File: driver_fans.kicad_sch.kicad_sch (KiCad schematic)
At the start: 8 parts, among them Q3 PMV60ENEAR

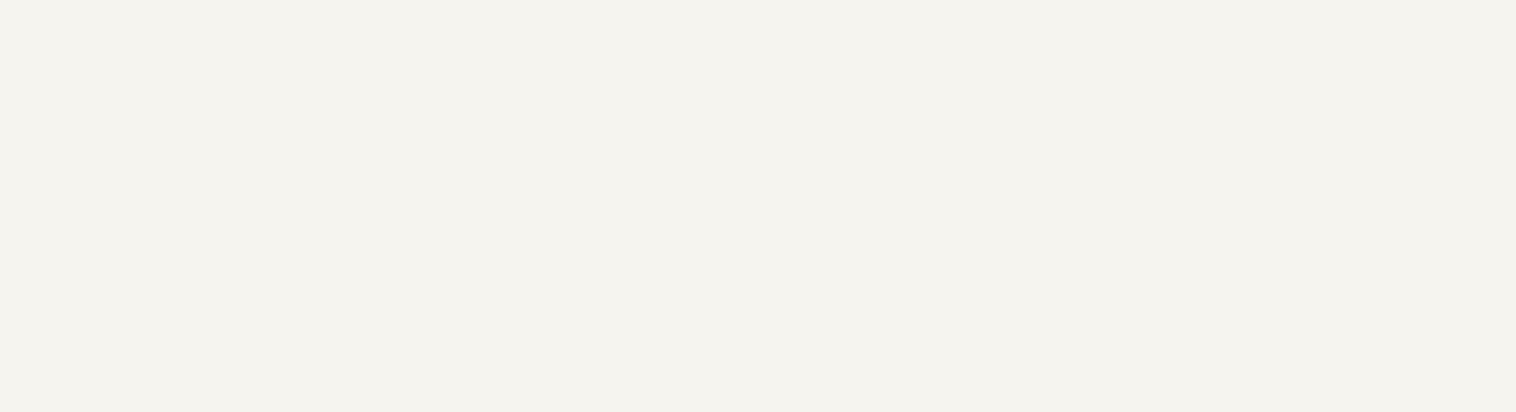
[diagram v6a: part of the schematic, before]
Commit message: added notes section to bottom of sheets
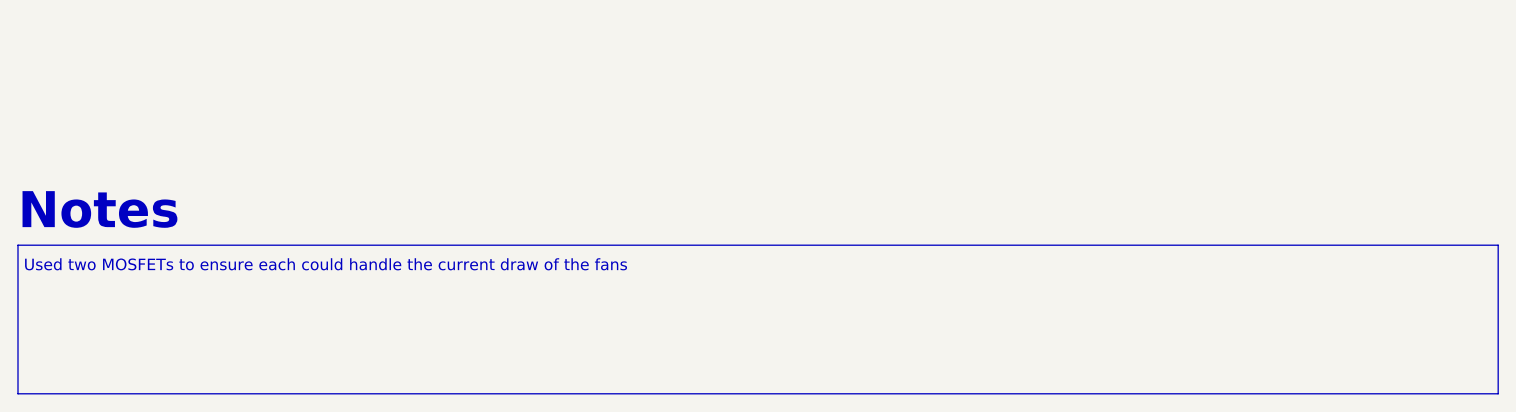
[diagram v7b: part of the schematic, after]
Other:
- note added: "Notes"
- note added: "Used two MOSFETs to ensure each could handle the current draw of the fans"
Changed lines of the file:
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@@
     (stroke (width 0) (type default))
+  )
+  (rectangle (start 12.065 181.61) (end 176.53 198.12)
+    (stroke (width 0) (type default))
+    (fill (type none))
+  )
+  (text "Used two MOSFETs to ensure each could handle the current draw of the fans"
+    (at 12.7 184.785 0)
+    (effects (font (size 1.27 1.27)) (justify left bottom))
   )
   (text "Driver Fans" (at 129.54 67.31 0)
     (effects (font (size 2.54 2.54) (thickness 0.508) bold) (justify left bottom))
   )
+  (text "Notes" (at 12.065 180.34 0)
+    (effects (font (size 4 4) (thickness 0.8) bold) (justify left bottom))
+  )
   (hierarchical_label "FAN_SIG_3V3" (shape input) (at 114.935 95.885 180) (fields_autoplaced)

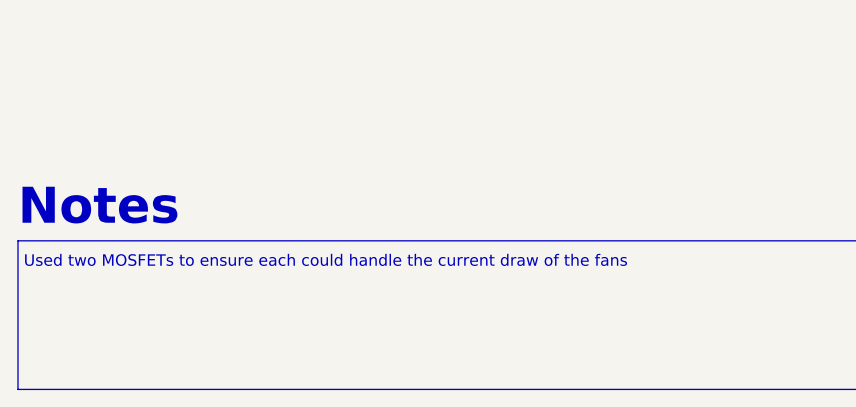
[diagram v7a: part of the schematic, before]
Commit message: Added to notes and changed resistor values
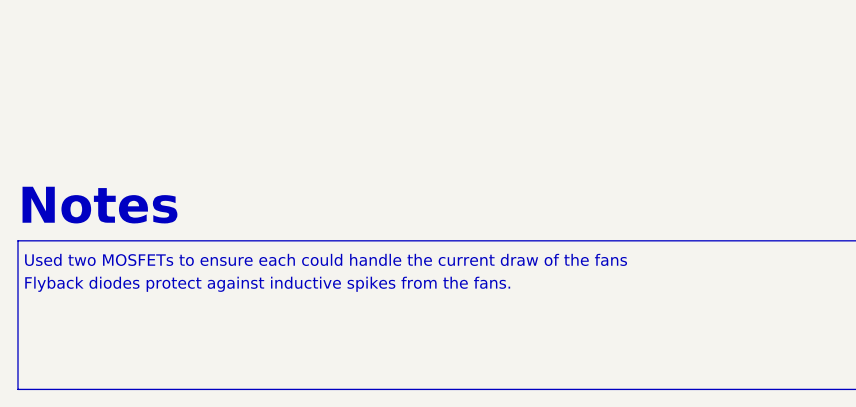
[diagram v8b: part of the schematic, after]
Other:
- note added: "Flyback diodes protect against inductive spikes from the fans."
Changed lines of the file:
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@@
     (effects (font (size 2.54 2.54) (thickness 0.508) bold) (justify left bottom))
+  )
+  (text "Flyback diodes protect against inductive spikes from the fans."
+    (at 12.7 187.325 0)
+    (effects (font (size 1.27 1.27)) (justify left bottom))
   )
   (text "Notes" (at 12.065 180.34 0)
